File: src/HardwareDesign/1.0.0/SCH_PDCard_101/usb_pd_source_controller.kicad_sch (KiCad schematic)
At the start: 41 parts, among them IC2 MCP22350T-2I/Q8X, IC3 INA219BIDCNT, T3 DMP3013SFV, T4 DMP3013SFV, T5 DMP3013SFV

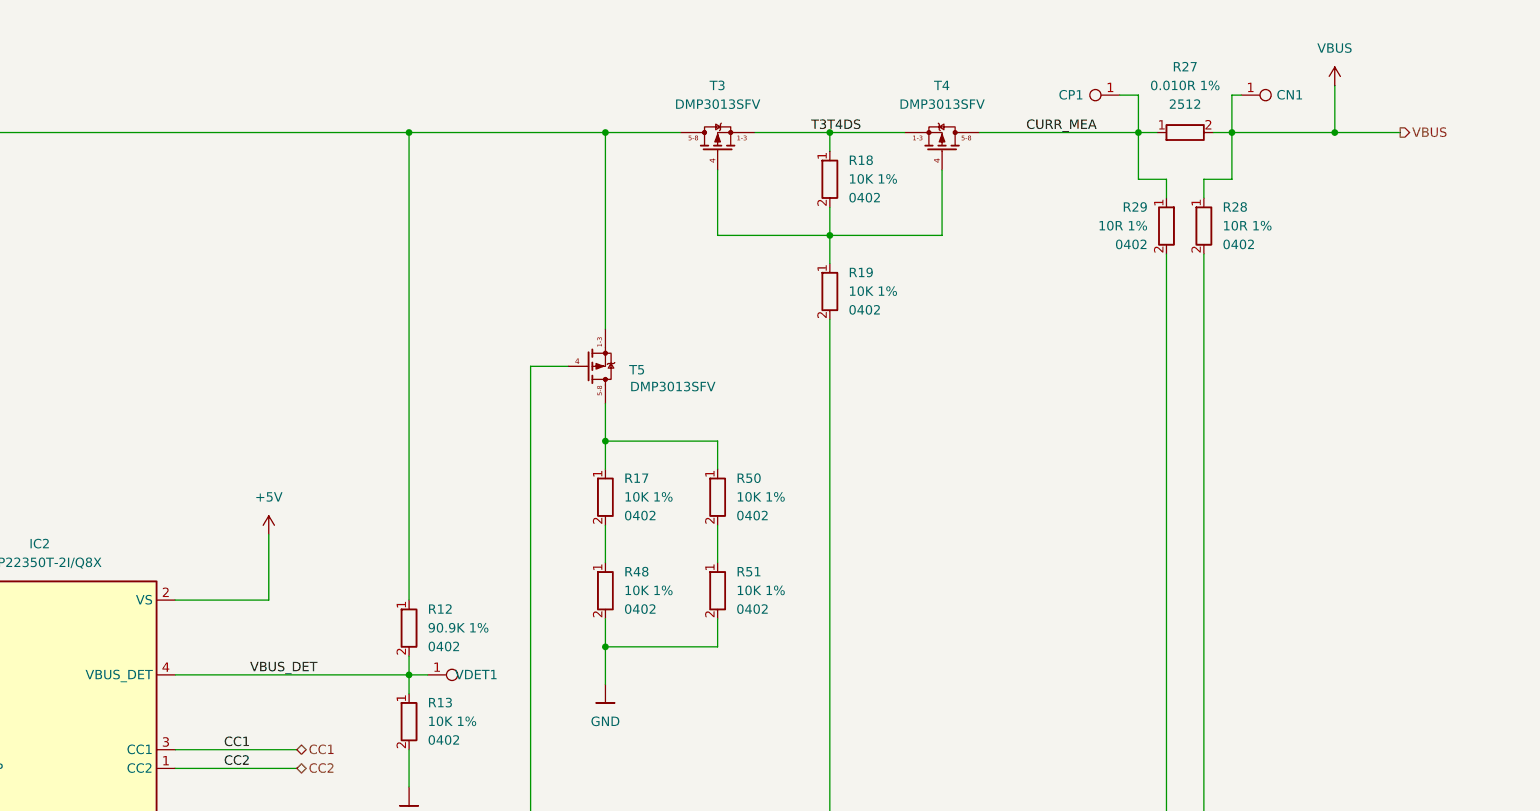
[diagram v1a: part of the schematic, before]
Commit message: Add bladecore to design
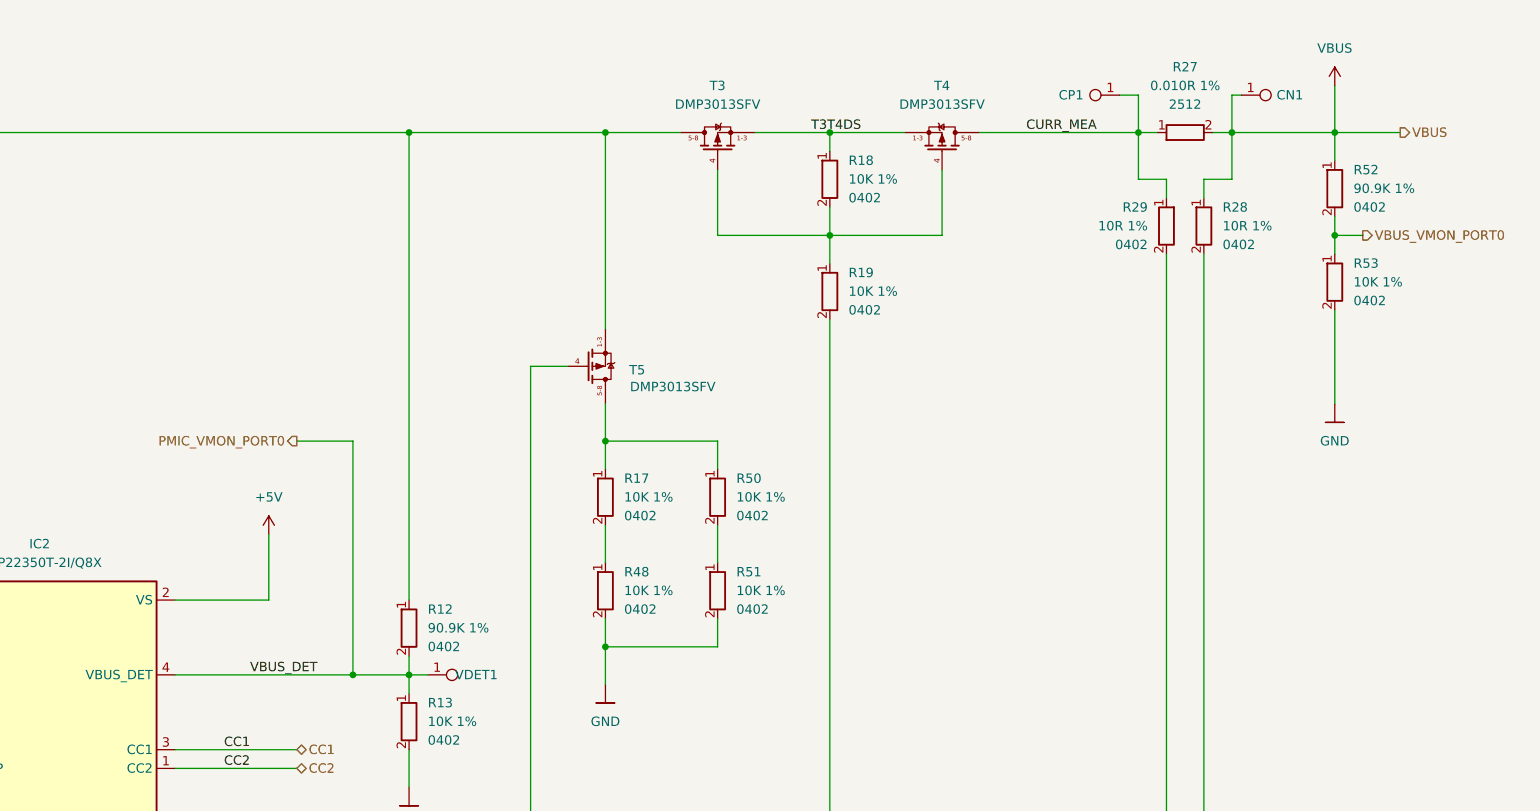
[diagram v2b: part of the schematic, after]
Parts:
- added R52: 90.9K 1%, Resistor_SMD:R_0402_1005Metric, symbol DS_Resistor_0402:90.9K 1% 0402
- added R53: 10K 1%, Resistor_SMD:R_0402_1005Metric, symbol DS_Resistor_0402:10K 1% 0402
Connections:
- net GND: now also R53.2
- net VBUS: now also R52.1
- net VBUS_DET renamed PMIC_VMON_PORT0
- new net VBUS_VMON_PORT0: R52.2, R53.1
